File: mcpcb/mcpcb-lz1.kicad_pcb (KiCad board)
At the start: 2 copper layers, 32 x 22 mm, 0 parts

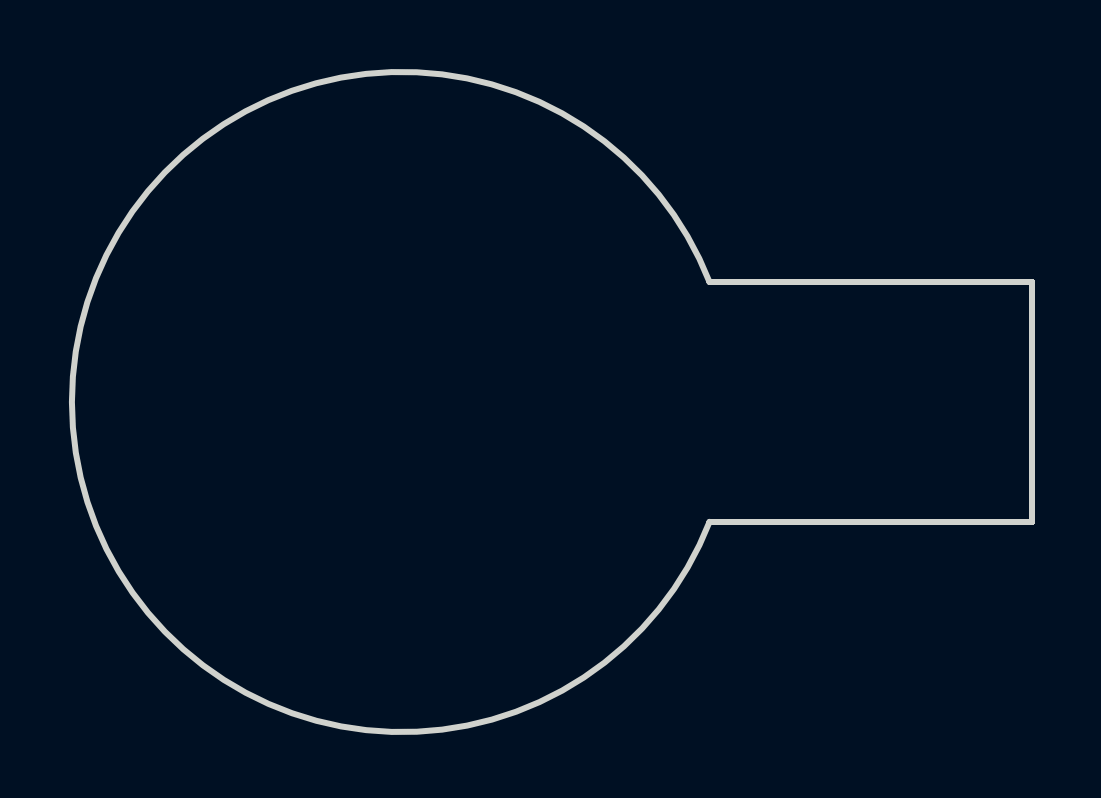
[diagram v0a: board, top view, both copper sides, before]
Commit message: mcpcb: routing
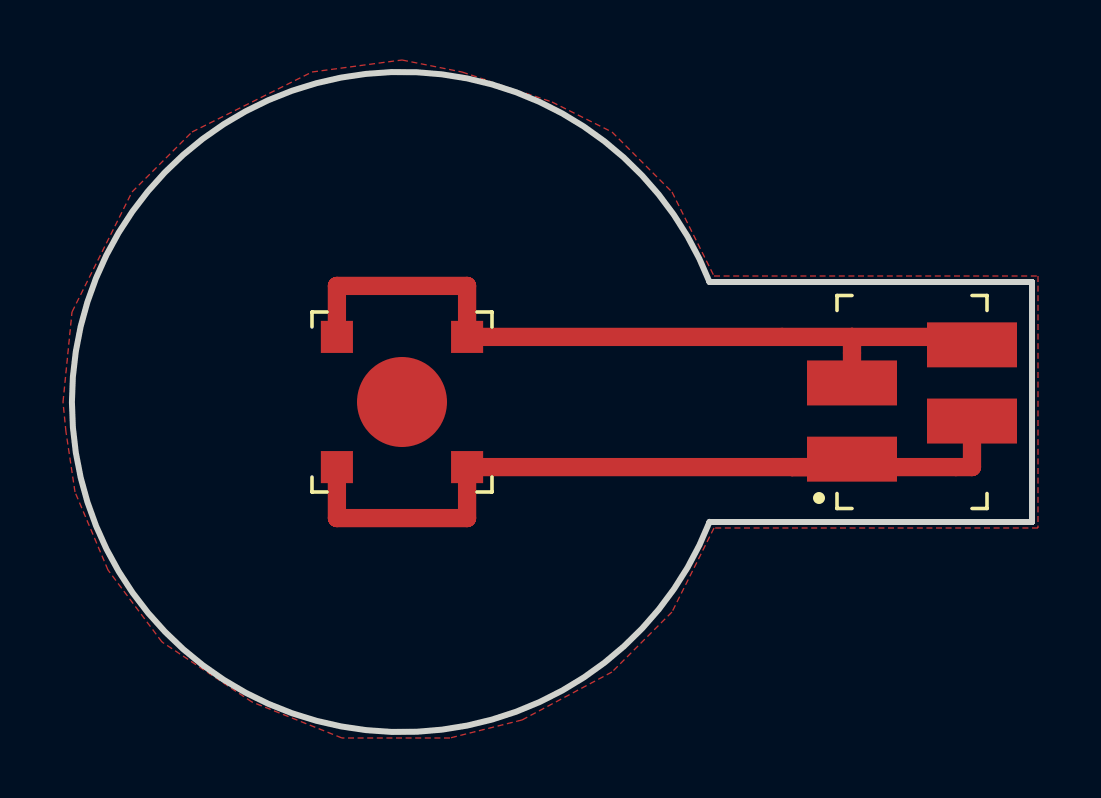
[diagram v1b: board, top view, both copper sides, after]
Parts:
- added ?: VAL**, generated:MicroMatch_4p, F.Cu at (17.0, 0.00)
- added ?: VAL**, powerled:ledengin-LZ1, F.Cu at (0.00, 0.00)
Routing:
- net (no net): track 0.00 -> 53.0 mm
- added copper zone on F.Cu, net (none)
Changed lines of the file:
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@@
     (thickness 1.6)
     (drawings 4)
-    (tracks 0)
+    (tracks 17)
     (zones 0)
-    (modules 0)
+    (modules 2)
     (nets 1)
   )
@@
     (last_trace_width 0.25)
     (trace_clearance 0.2)
-    (zone_clearance 0.508)
+    (zone_clearance 0.6096)
     (zone_45_only no)
     (trace_min 0.2)
@@
     (uvia_drill 0.1)
   )
+  (module generated:MicroMatch_4p (layer F.Cu)
+    (at 17 0 90)
+    (fp_text reference "" (at -4.45 0 180) (layer F.SilkS)
+      (effects (font (size 1 1) (thickness 0.15)))
+    )
+    (fp_text value VAL** (at 4.45 0 180) (layer F.Fab) hide
+      (effects (font (size 1 1) (thickness 0.15)))
+    )
+    (fp_line (start 2.8 -2) (end -2.8 -2) (layer F.Fab) (width 0.1))
+    (fp_line (start 2.8 2) (end 2.8 -2) (layer F.Fab) (width 0.1))
+    (fp_line (start -2.8 2) (end 2.8 2) (layer F.Fab) (width 0.1))
+    (fp_line (start -2.8 -2) (end -2.8 2) (layer F.Fab) (width 0.1))
+    (fp_line (start -3.55 -1.25) (end -3.55 -2.5) (layer F.Fab) (width 0.1))
+    (fp_line (start -2.8 -1.25) (end -3.55 -1.25) (layer F.Fab) (width 0.1))
+    (fp_line (start -2.8 1.25) (end -2.8 -1.25) (layer F.Fab) (width 0.1))
+    (fp_line (start -3.55 1.25) (end -2.8 1.25) (layer F.Fab) (width 0.1))
+    (fp_line (start -3.55 2.5) (end -3.55 1.25) (layer F.Fab) (width 0.1))
+    (fp_line (start 3.55 2.5) (end -3.55 2.5) (layer F.Fab) (width 0.1))
+    (fp_line (start 3.55 -2.5) (end 3.55 2.5) (layer F.Fab) (width 0.1))
+    (fp_line (start -3.55 -2.5) (end 3.55 -2.5) (layer F.Fab) (width 0.1))
+    (fp_line (start -3.55 2.5) (end -3.55 2) (layer F.SilkS) (width 0.12))
+    (fp_line (start -3.55 2.5) (end -3.05 2.5) (layer F.SilkS) (width 0.12))
+    (fp_line (start 3.55 2.5) (end 3.55 2) (layer F.SilkS) (width 0.12))
+    (fp_line (start 3.55 2.5) (end 3.05 2.5) (layer F.SilkS) (width 0.12))
+    (fp_line (start 3.55 -2.5) (end 3.55 -2) (layer F.SilkS) (width 0.12))
+    (fp_line (start 3.55 -2.5) (end 3.05 -2.5) (layer F.SilkS) (width 0.12))
+    (fp_line (start -3.55 -2.5) (end -3.55 -2) (layer F.SilkS) (width 0.12))
+    (fp_line (start -3.55 -2.5) (end -3.05 -2.5) (layer F.SilkS) (width 0.12))
+    (fp_line (start 3.55 -3.65) (end -3.55 -3.65) (layer F.CrtYd) (width 0.05))
+    (fp_line (start 3.55 3.65) (end 3.55 -3.65) (layer F.CrtYd) (width 0.05))
+    (fp_line (start -3.55 3.65) (end 3.55 3.65) (layer F.CrtYd) (width 0.05))
+    (fp_line (start -3.55 -3.65) (end -3.55 3.65) (layer F.CrtYd) (width 0.05))
+    (fp_circle (center -3.2 -3.1) (end -3.1 -3.1) (layer F.SilkS) (width 0.2))
+    (pad 4 smd rect (at 1.905 2 90) (size 1.5 3) (layers F.Cu F.Paste F.Mask))
+    (pad 2 smd rect (at -0.635 2 90) (size 1.5 3) (layers F.Cu F.Paste F.Mask))
+    (pad 3 smd rect (at 0.635 -2 90) (size 1.5 3) (layers F.Cu F.Paste F.Mask))
+    (pad 1 smd rect (at -1.905 -2 90) (size 1.5 3) (layers F.Cu F.Paste F.Mask))
+  )
+  (module powerled:ledengin-LZ1 (layer F.Cu)
+    (at 0 0 90)
+    (fp_text reference "" (at -5.4 0.6 180) (layer F.SilkS)
+      (effects (font (size 1 1) (thickness 0.15)))
+    )
+    (fp_text value VAL** (at 3.81 0 180) (layer F.Fab) hide
+      (effects (font (size 1 1) (thickness 0.15)))
+    )
+    (fp_line (start -3 3) (end -3 -3) (layer F.CrtYd) (width 0.12))
+    (fp_line (start 3 3) (end -3 3) (layer F.CrtYd) (width 0.12))
+    (fp_line (start 3 -3) (end 3 3) (layer F.CrtYd) (width 0.12))
+    (fp_line (start -3 -3) (end 3 -3) (layer F.CrtYd) (width 0.12))
+    (fp_circle (center 0 0) (end 0 1.6) (layer F.Fab) (width 0.15))
+    (fp_arc (start -2.2 2.2) (end -1.9 2.2) (angle -90) (layer F.Fab) (width 0.15))
+    (fp_arc (start -2.2 -2.2) (end -2.2 -1.9) (angle -90) (layer F.Fab) (width 0.15))
+    (fp_arc (start 2.2 -2.2) (end 1.9 -2.2) (angle -90) (layer F.Fab) (width 0.15))
+    (fp_arc (start 2.2 2.2) (end 1.9 2.2) (angle 90) (layer F.Fab) (width 0.15))
+    (fp_line (start -1.9 2.2) (end 1.9 2.2) (layer F.Fab) (width 0.15))
+    (fp_line (start -2.2 1.9) (end -2.2 -1.9) (layer F.Fab) (width 0.15))
+    (fp_line (start 2.2 -1.9) (end 2.2 1.9) (layer F.Fab) (width 0.15))
+    (fp_line (start -1.9 -2.2) (end 1.9 -2.2) (layer F.Fab) (width 0.15))
+    (fp_line (start -3 3) (end -3 2.5) (layer F.SilkS) (width 0.12))
+    (fp_line (start -3 3) (end -2.5 3) (layer F.SilkS) (width 0.12))
+    (fp_line (start 3 3) (end 3 2.5) (layer F.SilkS) (width 0.12))
+    (fp_line (start 3 3) (end 2.5 3) (layer F.SilkS) (width 0.12))
+    (fp_line (start 3 -3) (end 3 -2.5) (layer F.SilkS) (width 0.12))
+    (fp_line (start 3 -3) (end 2.5 -3) (layer F.SilkS) (width 0.12))
+    (fp_line (start -3 -3) (end -3 -2.5) (layer F.SilkS) (width 0.12))
+    (fp_line (start -3 -3) (end -2.5 -3) (layer F.SilkS) (width 0.12))
+    (pad 5 smd circle (at 0 0 90) (size 3 3) (layers F.Cu F.Paste F.Mask))
+    (pad 4 smd rect (at -2.17 2.17 90) (size 1.07 1.07) (layers F.Cu F.Paste F.Mask))
+    (pad 3 smd rect (at 2.17 2.17 90) (size 1.07 1.07) (layers F.Cu F.Paste F.Mask))
+    (pad 2 smd rect (at 2.17 -2.17 90) (size 1.07 1.07) (layers F.Cu F.Paste F.Mask))
+    (pad 1 smd rect (at -2.17 -2.17 90) (size 1.07 1.07) (layers F.Cu F.Paste F.Mask))
+  )
   (gr_line (start 21 4) (end 10.25 4) (layer Edge.Cuts) (width 0.2))
   (gr_line (start 21 -4) (end 21 4) (layer Edge.Cuts) (width 0.2))
   (gr_line (start 10.25 -4) (end 21 -4) (layer Edge.Cuts) (width 0.2))
   (gr_arc (start 0 0) (end 10.25 -4) (angle -317.4) (layer Edge.Cuts) (width 0.2))
+  (segment (start 2.17 2.17) (end 2.2 2.2) (width 0.25) (layer F.Cu) (net 0))
+  (segment (start 2.17 -2.17) (end 12.67 -2.17) (width 0.6096) (layer F.Cu) (net 0) (status 40000))
+  (segment (start 2.17 -2.17) (end 2.17 -3.87) (width 0.6096) (layer F.Cu) (net 0))
+  (segment (start -2.17 2.17) (end -2.17 3.87) (width 0.6096) (layer F.Cu) (net 0))
+  (segment (start 2.17 2.17) (end 2.17 3.87) (width 0.6096) (layer F.Cu) (net 0))
+  (segment (start 15 -1.635) (end 15 -2.17) (width 0.6096) (layer F.Cu) (net 0))
+  (segment (start 15 -0.635) (end 15 -1.635) (width 0.6096) (layer F.Cu) (net 0))
+  (segment (start 17.985 -2.17) (end 15 -2.17) (width 0.6096) (layer F.Cu) (net 0))
+  (segment (start 15 -2.17) (end 12.67 -2.17) (width 0.6096) (layer F.Cu) (net 0))
+  (segment (start 18.465 2.17) (end 13 2.17) (width 0.6096) (layer F.Cu) (net 0))
+  (segment (start 19 0.635) (end 19 2.17) (width 0.6096) (layer F.Cu) (net 0))
+  (segment (start 2.17 2.17) (end 13 2.17) (width 0.6096) (layer F.Cu) (net 0))
+  (segment (start 13 2.17) (end 14.735 2.17) (width 0.6096) (layer F.Cu) (net 0))
+  (segment (start -2.17 -2.17) (end -2.17 -3.87) (width 0.6096) (layer F.Cu) (net 0))
+  (segment (start -2.17 3.87) (end 2.17 3.87) (width 0.6096) (layer F.Cu) (net 0))
+  (segment (start -2.17 -3.87) (end 2.17 -3.87) (width 0.6096) (layer F.Cu) (net 0))
+  (segment (start 19 2.17) (end 18.465 2.17) (width 0.6096) (layer F.Cu) (net 0))
+  (zone (net 0) (net_name "") (layer F.Cu) (hatch full 0.508)
+    (connect_pads (clearance 0.6096))
+    (min_thickness 0.254)
+    (fill yes (mode segment) (arc_segments 16) (thermal_gap 0.508) (thermal_bridge_width 0.508))
+    (polygon
+      (pts
+        (xy -11.3 0) (xy -11 -3) (xy -9 -7) (xy -7 -9) (xy -3 -11)
+        (xy 0 -11.4) (xy 2 -11) (xy 5 -10) (xy 7 -9) (xy 9 -7)
+        (xy 10.4 -4.2) (xy 21.2 -4.2) (xy 21.2 4.2) (xy 10.4 4.2) (xy 9 7)
+        (xy 7 9) (xy 4 10.6) (xy 1.6 11.2) (xy 0 11.2) (xy -2 11.2)
+        (xy -5 10) (xy -8 8) (xy -9.8 5.6) (xy -10.9 3) (xy -11.2 1)
+      )
+    )
+  )
 )

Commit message: mcpcb: update layout, add filled zone
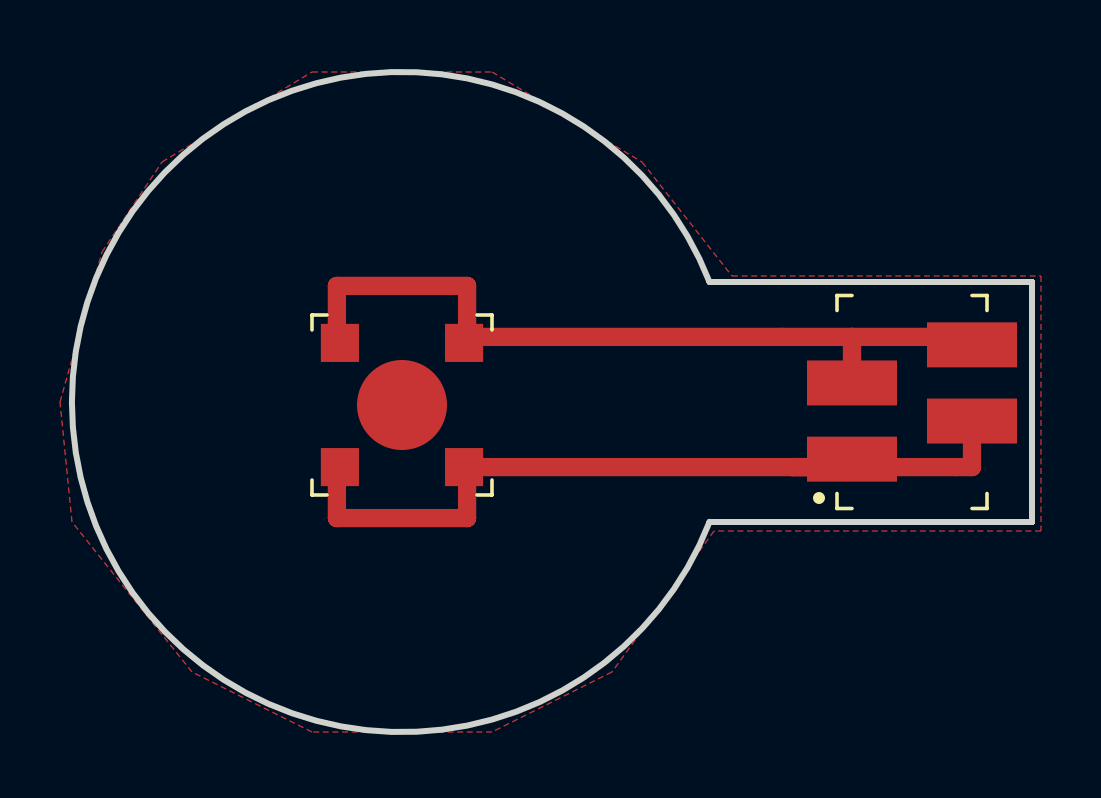
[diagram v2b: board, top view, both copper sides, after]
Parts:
- removed ?: VAL**, generated:MicroMatch_4p
- removed ?: VAL**, powerled:ledengin-LZ1
- added J1: CONN_01X04, generated:MicroMatch_4p, F.Cu at (17.0, 0.00)
- added L1: LED, powerled:ledengin-LZ1-m, F.Cu at (0.00, 0.10)
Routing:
- net (no net): track 53.0 -> 0.00 mm
- net S1: track 0.00 -> 27.9 mm
- net S2: track 0.00 -> 25.1 mm
